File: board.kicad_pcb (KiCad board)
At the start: 2 copper layers, 92 x 72 mm, 50 parts, among them J1 LASER, J10 Mode, J11 Y, J12 12V, J13 Y, J14 X, J15 12V-36V, J16 CNC_OUT2, J2 Pololu_Breakout_A4988, J3 V_LASER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

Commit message: Reduce DRC
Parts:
- moved C3 0.54 mm to (140.7, 99.5)
- moved C2 0.16 mm to (128.5, 99.5)
- turned C5 to 270 degrees
- turned R6 to 90 degrees
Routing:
- net /D5: track 0.00 -> 59.5 mm
- net /D2: track 0.00 -> 45.9 mm
- net /D4: track 0.00 -> 45.7 mm
- net /D7: track 0.00 -> 39.4 mm
- net /D6: track 0.00 -> 37.2 mm
- net /D3: track 0.00 -> 35.5 mm
- net /D8: track 41.2 -> 57.7 mm
- net Net-(C5-Pad2): track 0.00 -> 15.5 mm
- net Net-(C5-Pad1): track 14.3 -> 0.00 mm
- net /V_STEP_MOT: track 139.5 -> 126.5 mm
- net GND: track 0.00 -> 11.0 mm, vias 7 -> 11
- net /V_LASER: track 65.4 -> 73.4 mm
- net +5V: track 223.1 -> 227.1 mm
- net Net-(J11-Pad1): track 38.2 -> 35.3 mm
- net Net-(J11-Pad2): track 35.9 -> 33.2 mm
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
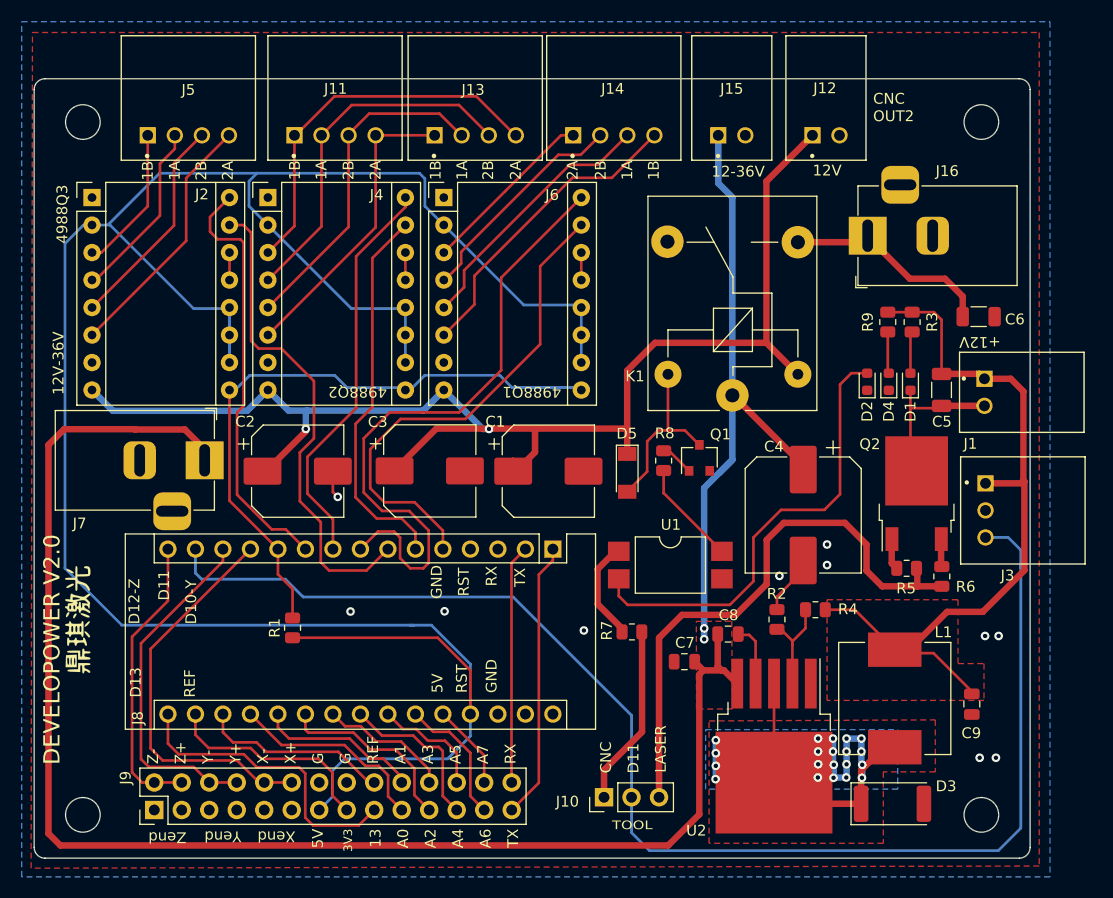
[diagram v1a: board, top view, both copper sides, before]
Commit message: Merge main 12V networks
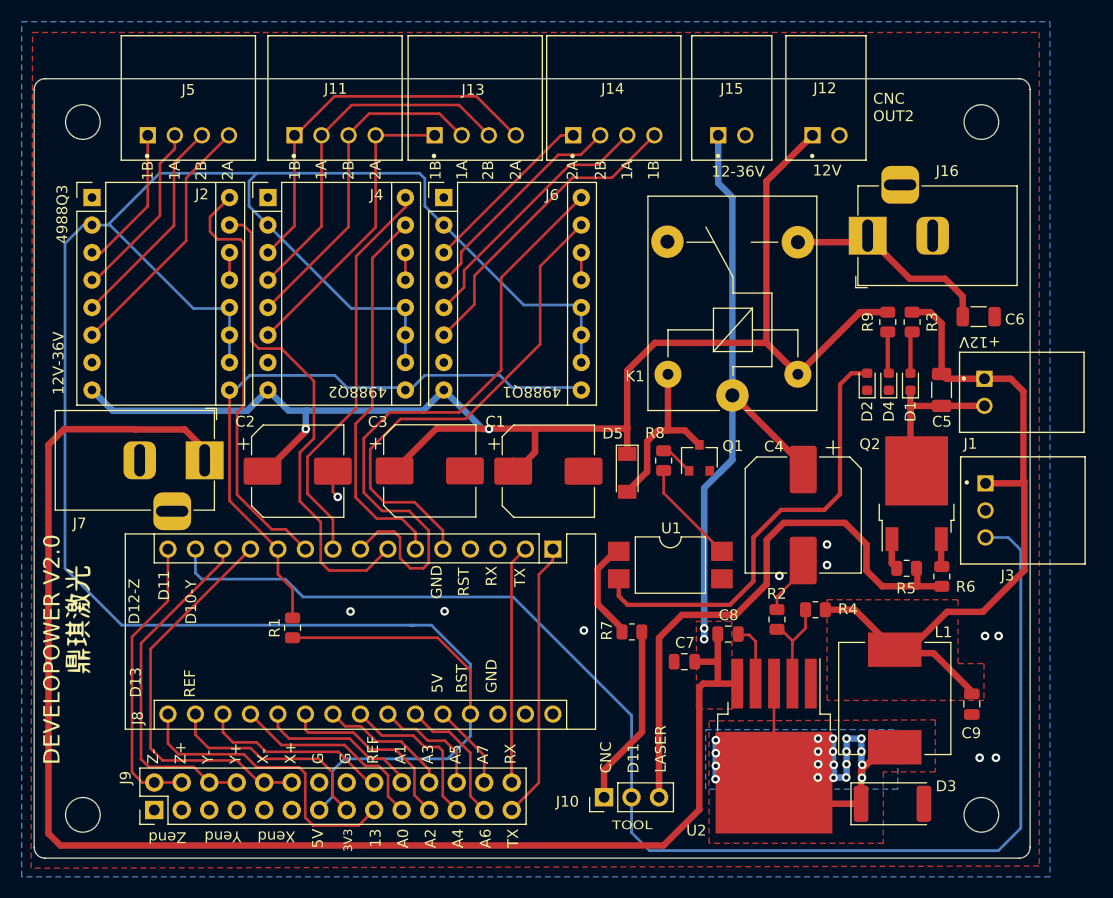
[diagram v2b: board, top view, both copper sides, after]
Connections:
- net /relay.p5 renamed /spindle_ctl
- C1 pad 1: /V_STEP_MOT -> +12V
- C2 pad 1: /V_STEP_MOT -> +12V
- C3 pad 1: /V_STEP_MOT -> +12V
- C5 pad 1: /V_LASER -> +12V
- C9 pad 1: /V_LASER -> +12V
- D5 pad 1: /V_STEP_MOT -> +12V
- J1 pad 1: /V_LASER -> +12V
- J12 pad 1: /V_STEP_MOT -> +12V
- J2 pad 8: /V_STEP_MOT -> +12V
- J3 pad 1: /V_LASER -> +12V
- J4 pad 8: /V_STEP_MOT -> +12V
- J6 pad 8: /V_STEP_MOT -> +12V
- K1 pad 2: /V_STEP_MOT -> +12V
- L1 pad 2: /V_LASER -> +12V
- R3 pad 1: /V_LASER -> +12V
- R4 pad 1: /V_LASER -> +12V
- R9 pad 1: /V_LASER -> +12V
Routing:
- net +12V: track 0.00 -> 208.8 mm, vias 0 -> 2
- net /V_STEP_MOT: track 126.5 -> 0.00 mm, vias 2 -> 0
- net /V_LASER: track 73.4 -> 0.00 mm
- added copper zone on F.Cu, net +12V
- removed copper zone on F.Cu, net /V_LASER

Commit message: Improve parts placement
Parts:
- removed H3: MountingHole, MountingHole:MountingHole_3.2mm_M3
- moved J6 2.64 mm to (144.4, 73.3)
- moved J10 2.25 mm to (154.6, 129.7)
- moved J9 1.85 mm to (115.2, 129.0)
- moved C3 1.84 mm to (140.4, 97.7)
- moved J8 1.83 mm to (150.9, 105.3)
- moved C1 1.81 mm to (151.9, 97.7)
- moved C2 1.81 mm to (128.7, 97.7)
- moved J11 1.79 mm to (130.6, 67.4)
- moved J4 1.70 mm to (127.2, 73.3)
- moved J13 1.68 mm to (143.7, 67.4)
- moved J7 1.62 mm to (121.0, 97.3)
- moved J16 1.52 mm to (180.3, 76.5)
- moved J5 1.47 mm to (117.5, 67.4)
- moved J14 1.47 mm to (156.8, 67.4)
- moved J15 1.11 mm to (169.1, 67.5)
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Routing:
- net /D5: track 59.5 -> 49.8 mm
- net +12V: track 208.8 -> 199.7 mm, vias 2 -> 3
- net /D2: track 45.9 -> 38.9 mm
- net +5V: track 227.1 -> 220.3 mm
- net Net-(D3-Pad1): track 47.6 -> 44.2 mm
- net /D11: track 126.1 -> 129.3 mm
- net /D8: track 57.7 -> 60.8 mm
- net /D7: track 39.4 -> 36.3 mm
- net /D4: track 45.7 -> 43.0 mm
- net /D3: track 35.5 -> 33.0 mm
- net Net-(J14-Pad2): track 20.6 -> 19.2 mm
- net /D6: track 37.2 -> 35.8 mm
- net /A0: track 18.8 -> 20.1 mm
- net Net-(J14-Pad3): track 24.5 -> 23.3 mm
- net Net-(J11-Pad1): track 35.3 -> 36.4 mm
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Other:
- board size 92 x 72 mm -> 92 x 72.2 mm

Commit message: Power on the Arduino
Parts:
- added H3: MountingHole, MountingHole:MountingHole_3.2mm_M3, F.Cu at (108.0, 131.5)
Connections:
- J8 pad 30: (no net) -> +12V
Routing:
- net +12V: track 199.7 -> 225.8 mm

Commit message: Update using Kicad 5.1.12
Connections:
- net /D11 renamed /D11_TOOL

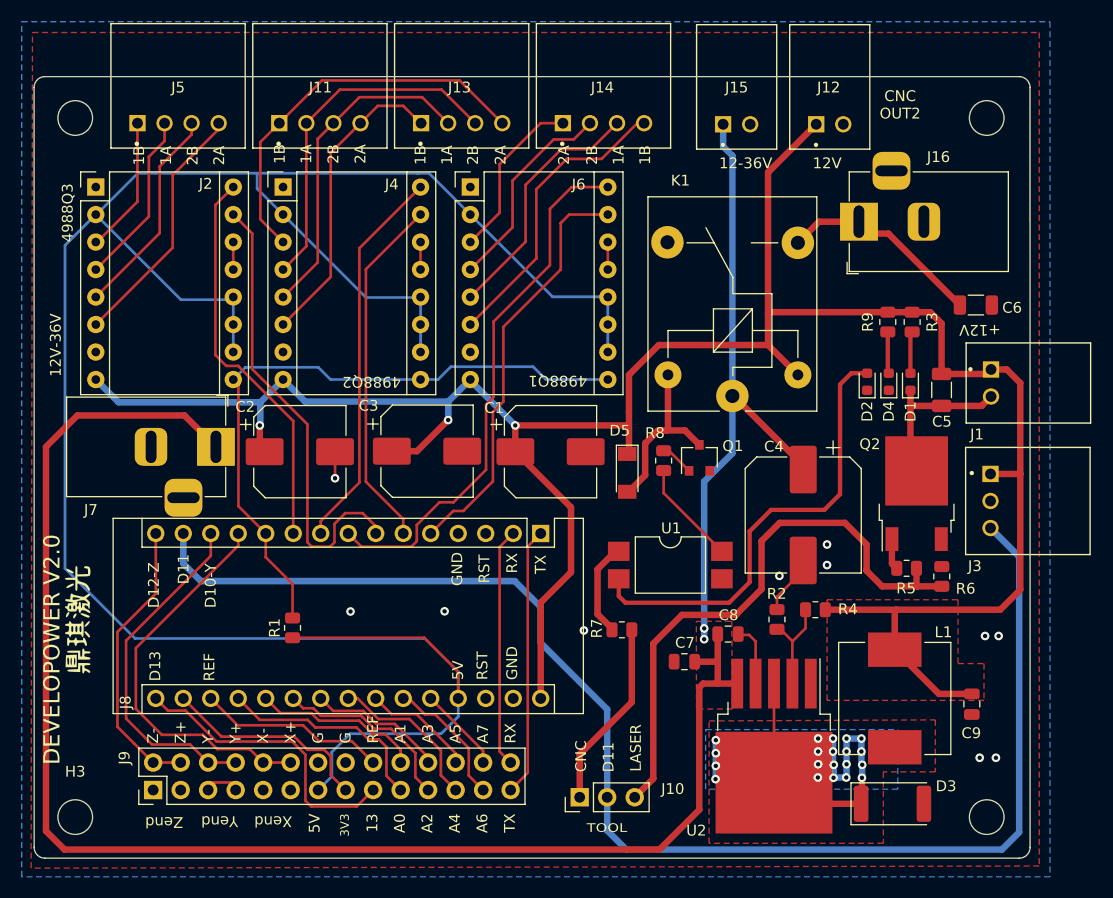
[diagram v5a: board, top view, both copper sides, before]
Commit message: Convert project to Kicad v6
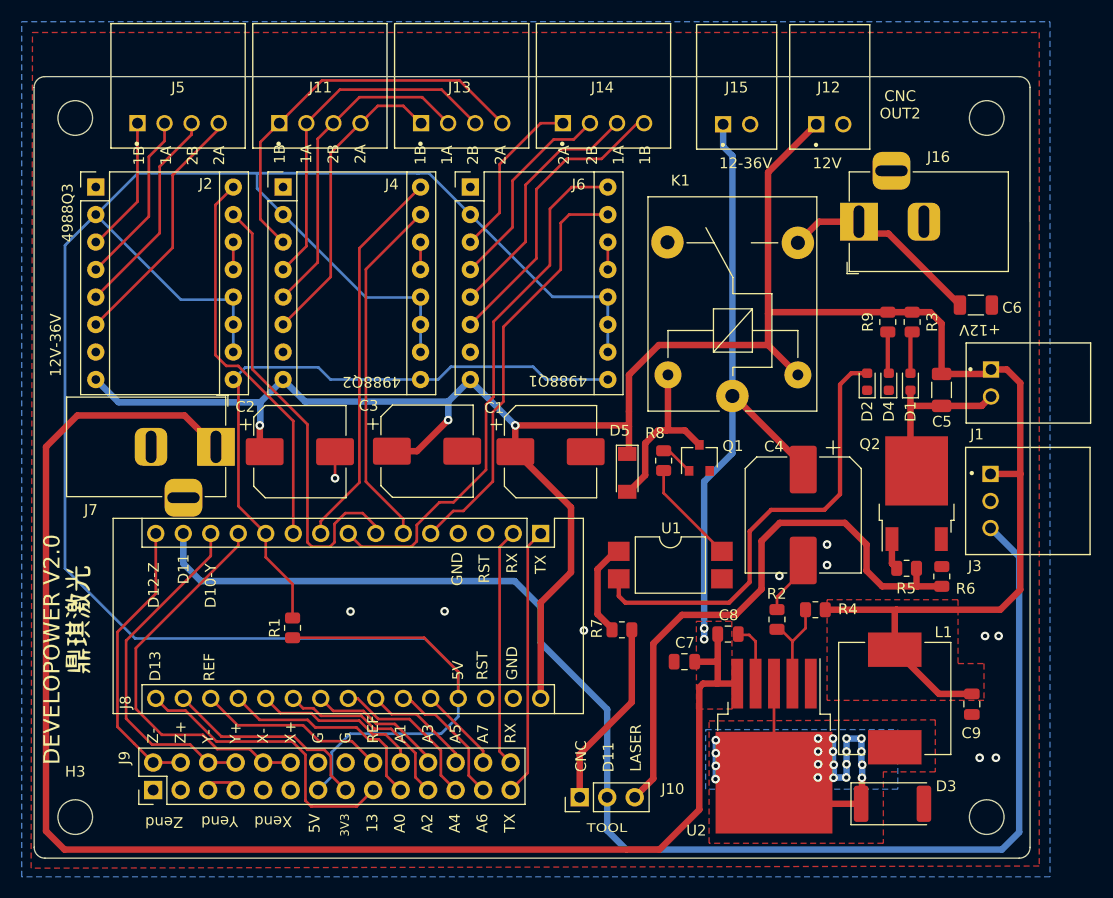
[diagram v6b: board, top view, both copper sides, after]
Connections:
- J8 pad 28: (no net) -> unconnected-(J8-Pad28)
- J8 pad 3: (no net) -> unconnected-(J8-Pad3)
- K1 pad 4: (no net) -> unconnected-(K1-Pad4)
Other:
- net class Default removed
- net class Power removed
